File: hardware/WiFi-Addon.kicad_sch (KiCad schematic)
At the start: 31 parts, among them J1 PWR, J3 USB_B_Micro, U1 AMS1117-3.3, U2 ESP-12F, U3 CH340G

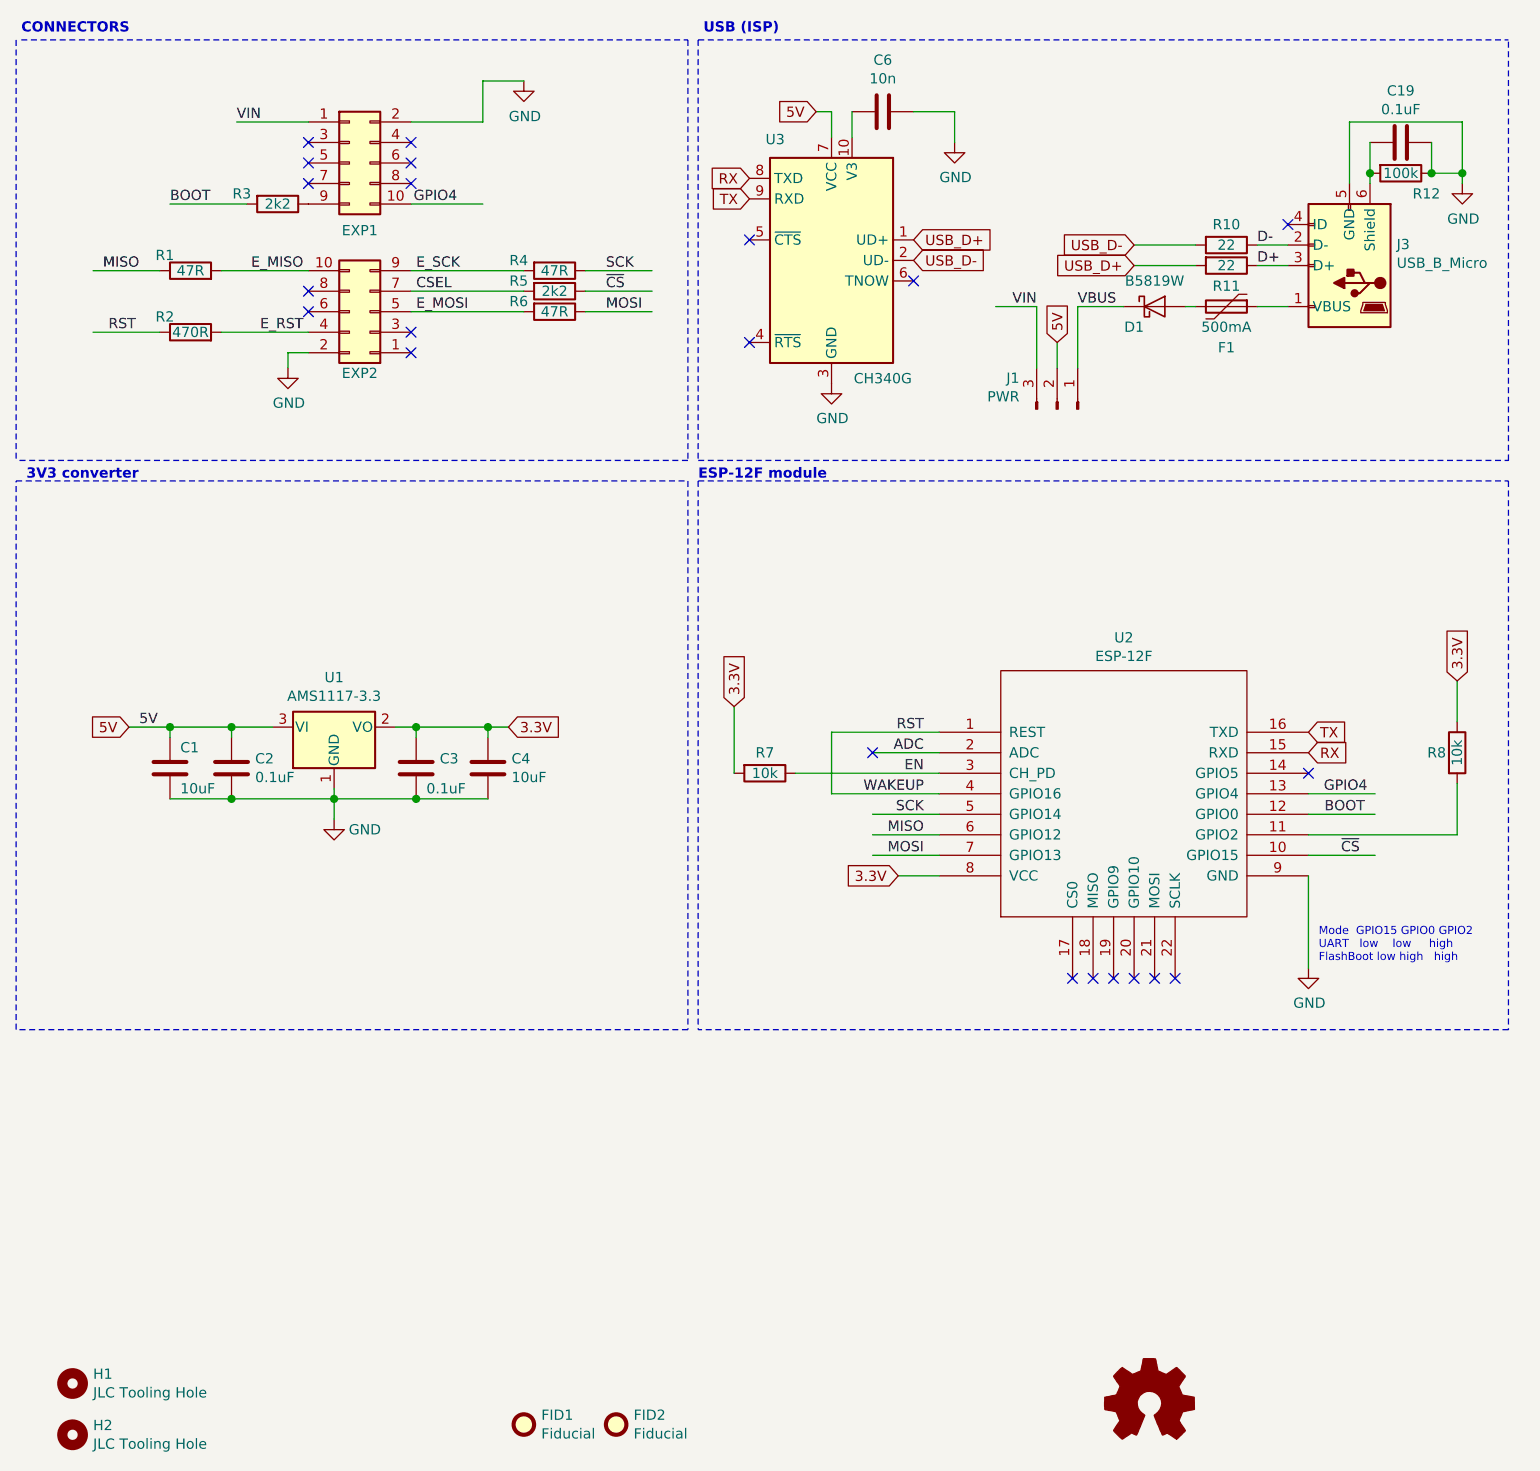
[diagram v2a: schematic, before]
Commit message: Added some more information to schema
Added datasheet links to ESP-12F and ESP8266EX
Some additional info on schematics and repositioning of resistors for better understed of their purpose.
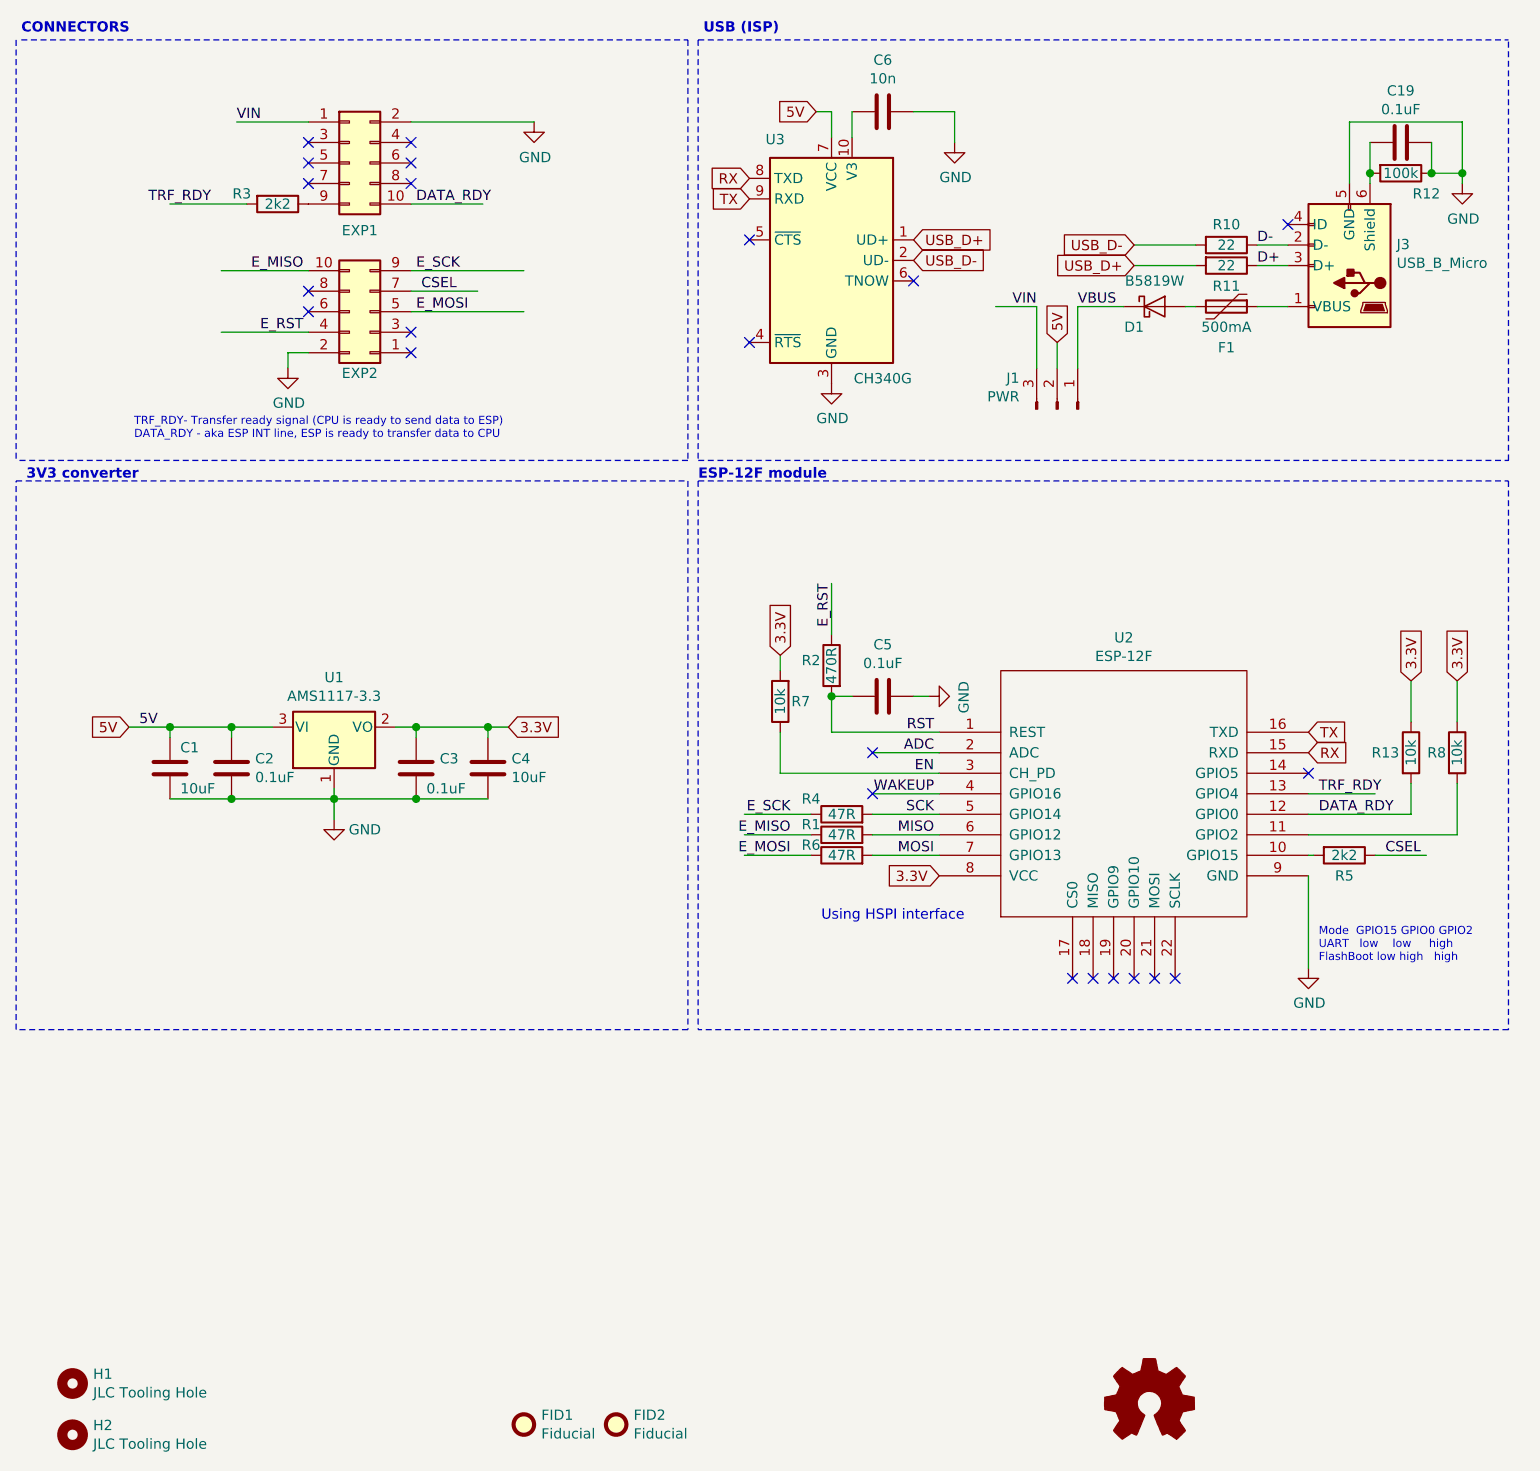
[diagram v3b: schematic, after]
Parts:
- added C5: 0.1uF, PrntrBoardV2:C_0603_1608Metric, symbol Device:C
- added R13: 10k, PrntrBoardV2:R_0603_1608Metric, symbol Device:R
- U2: ESP datasheet (none) -> https://www.espressif.com/sites/default/files/documentation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
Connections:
- net 3.3V: now also R13.1
- net CSEL: now also R5.1; no longer R5.2
- net E_MISO: now also R1.1; no longer R1.2
- net E_MOSI: now also R6.1; no longer R6.2
- net E_RST: now also R2.1; no longer R2.2
- net E_SCK: now also R4.1; no longer R4.2
- net GND: now also C5.1
- net MISO: now also R1.2; no longer R1.1
- net MOSI: now also R6.2; no longer R6.1
- net RST: now also R2.2, C5.2; no longer R2.1, U2.4 (GPIO16)
- net SCK: now also R4.2; no longer R4.1
- net BOOT renamed DATA_RDY
- net DATA_RDY: now also EXP1.10 (Pin_10), R13.2; no longer R3.2
- net GPIO4 renamed TRF_RDY
- net TRF_RDY: now also R3.2; no longer EXP1.10 (Pin_10)
- net ~CS: no longer names the net of U2.10 (GPIO15)
- net ~CS: now also R5.2; no longer R5.1
- new net WAKEUP: U2.4 (GPIO16)
- no-connect marks 22 -> 23
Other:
- note added: "TRF_RDY- Transfer ready signal (CPU is ready to send data to ESP) DATA_RDY - aka ESP INT line, ESP is ready to transfer data to CPU"
- note added: "Using HSPI interface"
- moved on the sheet: R1, R2, R4, R5, R6, R7
